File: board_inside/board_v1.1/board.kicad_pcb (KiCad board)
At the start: 2 copper layers, 79.9 x 68.3 mm, 116 parts, among them J1 PJ-063AH, J2 Raspberry_Pi_Zero_W, J3 Conn_01x04_Female, J4 Conn_01x06_Female, J5 QR_connector, M1 Stepper_Motor_bipolar, Q1 BC848, SW1 PB, U1 DCF1-Pollin, U10 TLV8811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

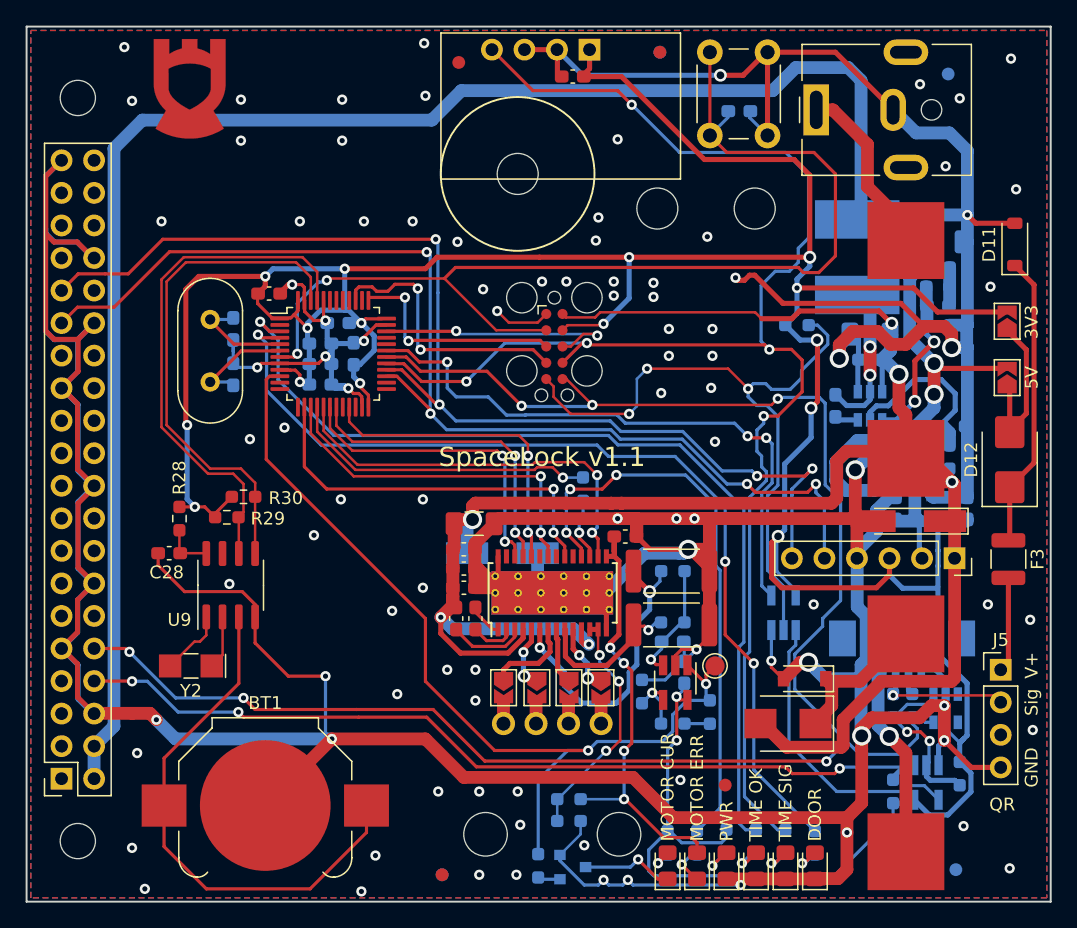
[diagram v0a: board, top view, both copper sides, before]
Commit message: board v1.1: clean up, create own folder
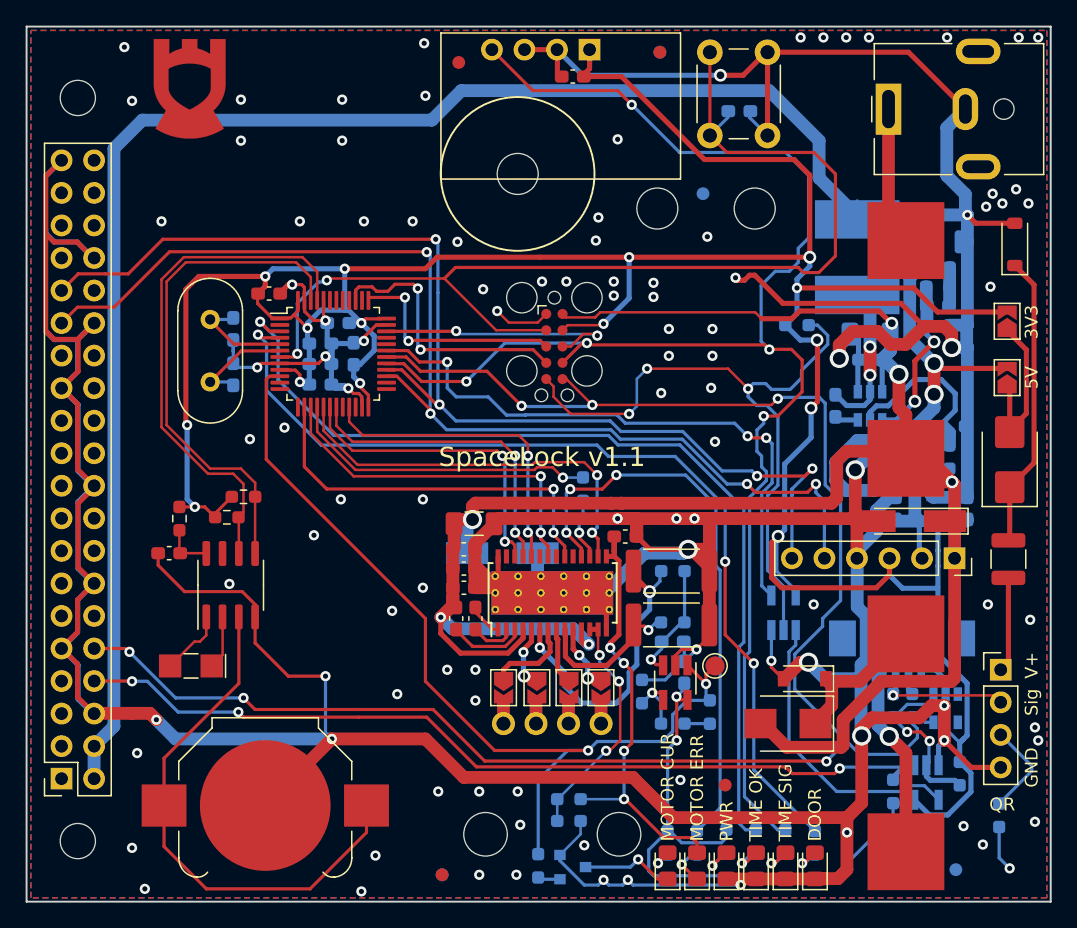
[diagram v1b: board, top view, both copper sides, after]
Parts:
- added R31: 10k, Resistor_SMD:R_0603_1608Metric_Pad0.98x0.95mm_HandSolder, B.Cu at (179.6, 130.6)
- BT1: value CR3212 -> CR2032
- F3: value Polyfuse_Small -> Polyfuse 200mA
- moved FID5 21.3 mm to (156.5, 82.0)
- moved J1 5.64 mm to (170.9, 75.4)
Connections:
- J5 pad 3: unconnected-(J5-Pin_3-Pad3) -> Net-(J5-Pin_3)
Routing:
- net Net-(J5-Pin_3): track 0.00 -> 7.72 mm
- net GND: track 638.5 -> 645.1 mm, vias 98 -> 108
- net +5V: track 184.5 -> 178.3 mm
- net /+12V_UNFUSED: track 14.6 -> 11.5 mm
